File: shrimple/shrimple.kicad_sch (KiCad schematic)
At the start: 105 parts, among them U1 ProMicro

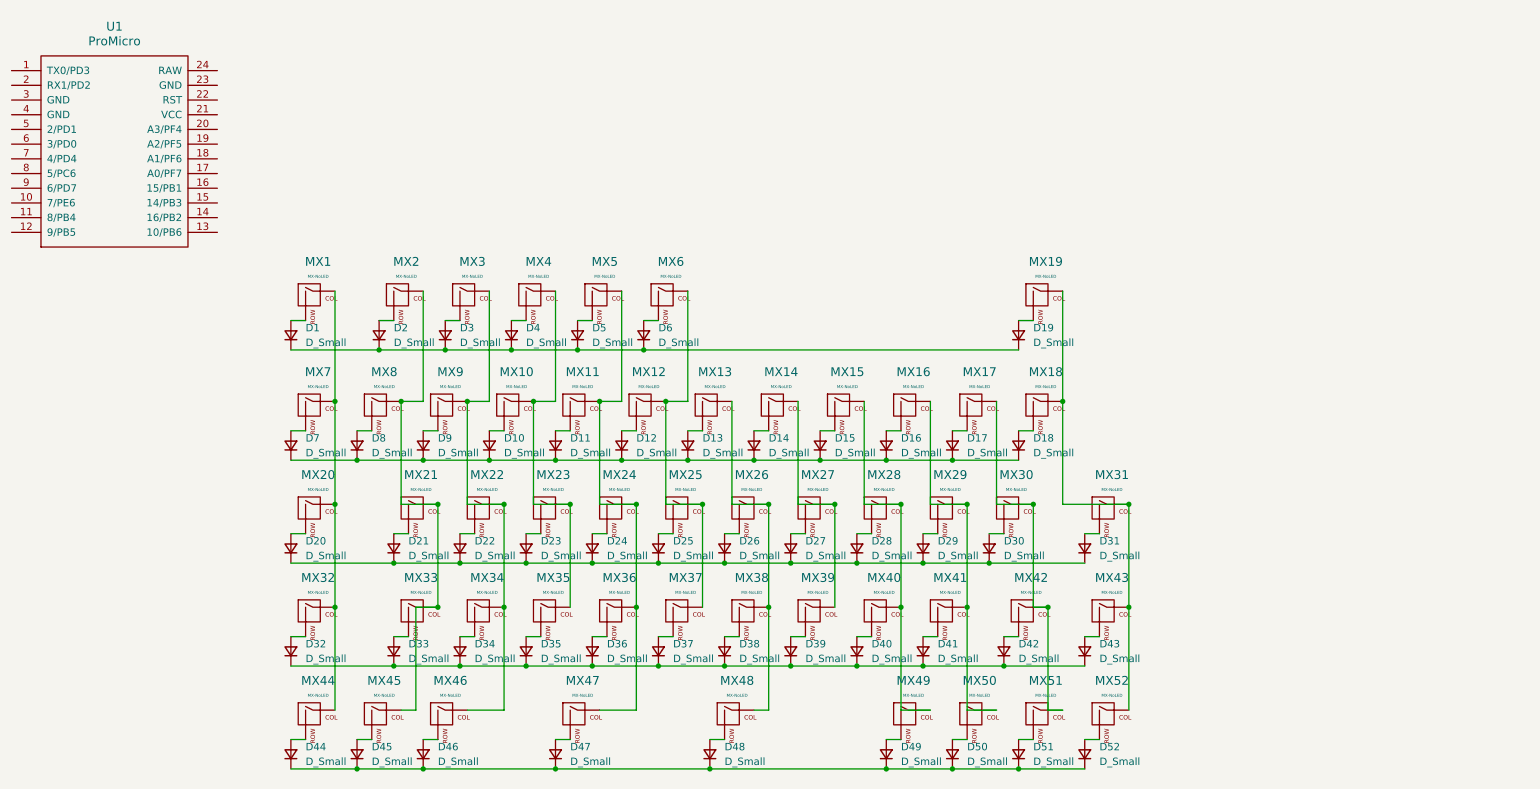
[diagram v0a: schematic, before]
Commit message: updated schematic and placed footprints
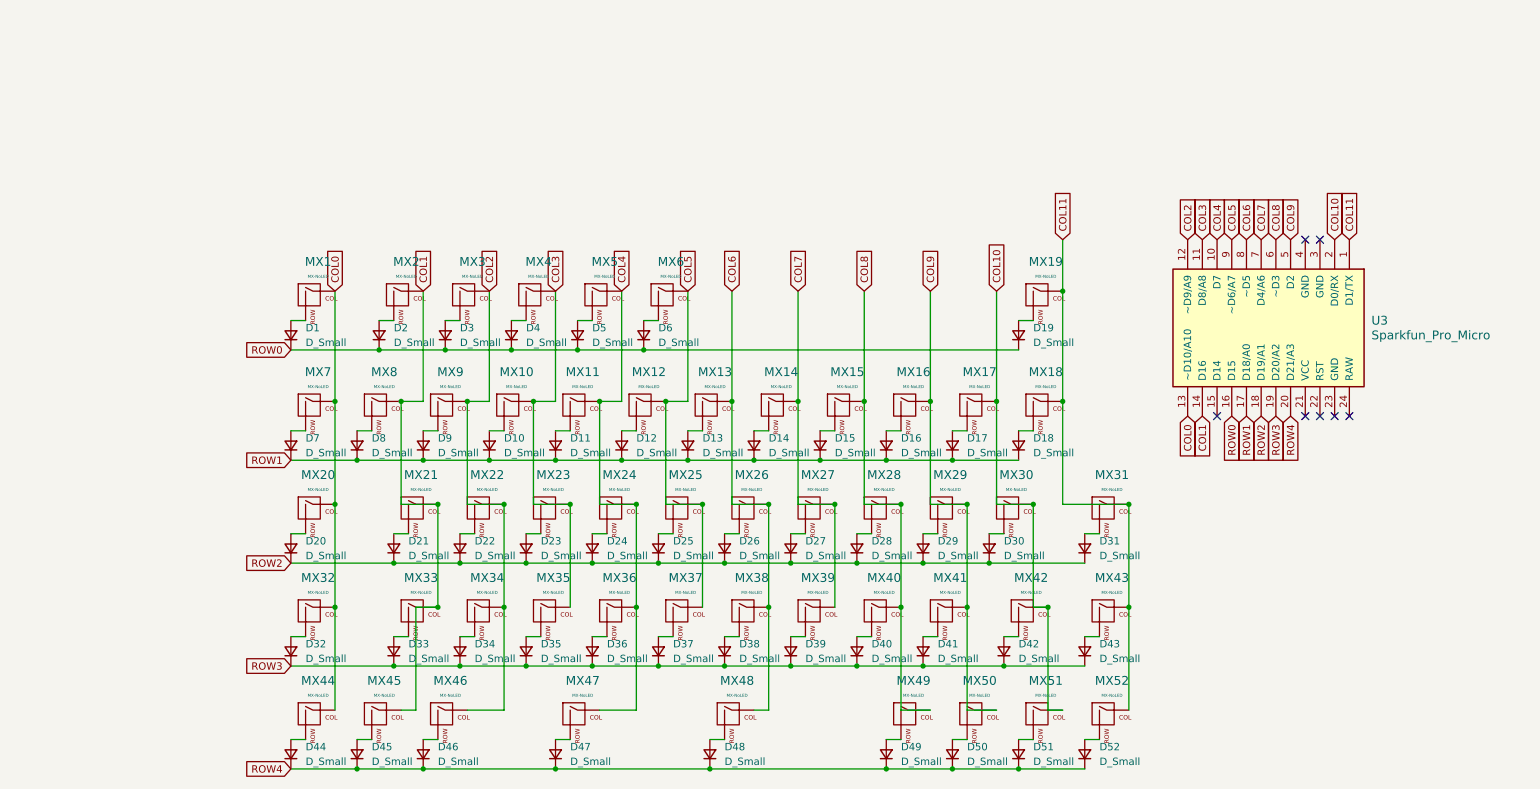
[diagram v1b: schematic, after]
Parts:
- removed U1: ProMicro, symbol keebio:ProMicro
- added U3: Sparkfun_Pro_Micro, arduino:Sparkfun_Pro_Micro, symbol arduino:Sparkfun_Pro_Micro
- D1, D10, D11, D12, D13, D14, D15, D16, D17, D18, D19, D2, D20, D21, D22, D23, D24, D25, D26, D27, D28, D29, D3, D30, D31, D32, D33, D34, D35, D36, D37, D38, D39, D4, D40, D41, D42, D43, D44, D45, D46, D47, D48, D49, D5, D50, D51, D52, D6, D7, D8, D9: footprint (none) -> Diode_SMD:D_SOD-123
- MX1, MX10, MX11, MX12, MX13, MX14, MX15, MX16, MX17, MX18, MX19, MX2, MX21, MX22, MX23, MX24, MX25, MX26, MX27, MX28, MX29, MX3, MX30, MX33, MX34, MX35, MX36, MX37, MX38, MX39, MX4, MX40, MX41, MX43, MX45, MX49, MX5, MX50, MX51, MX52, MX6, MX7, MX8, MX9: footprint (none) -> hybrids:MX-1U-NoLED
- MX20, MX31: footprint (none) -> hybrids:MX-1.5U-NoLED
- MX32: footprint (none) -> hybrids:MX-1.75U-NoLED
- MX42, MX44, MX46: footprint (none) -> hybrids:MX-1.25U-NoLED
- MX47: footprint (none) -> hybrids:MX-2.25U-ReversedStabilizers-NoLED
- MX48: footprint (none) -> hybrids:MX-2.75U-ReversedStabilizers-NoLED
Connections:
- net COL0: now reaches MX1.1 (COL), MX20.1 (COL), MX32.1 (COL), MX44.1 (COL), MX7.1 (COL)
- net COL0: now also U3.13 (~D10/A10)
- net COL3: now reaches MX10.1 (COL), MX23.1 (COL), MX35.1 (COL), MX4.1 (COL)
- net COL3: now also U3.11 (D8/A8)
- net ROW3: now reaches D32.1 (K), D33.1 (K), D34.1 (K), D35.1 (K), D36.1 (K), D37.1 (K), D38.1 (K), D39.1 (K), D40.1 (K), D41.1 (K), D42.1 (K), D43.1 (K)
- net ROW3: now also U3.19 (D20/A2)
- net ROW0: now reaches D1.1 (K), D19.1 (K), D2.1 (K), D3.1 (K), D4.1 (K), D5.1 (K), D6.1 (K)
- net ROW0: now also U3.16 (D15)
- net COL4: now reaches MX11.1 (COL), MX24.1 (COL), MX36.1 (COL), MX47.1 (COL), MX5.1 (COL)
- net COL4: now also U3.10 (D7)
- net COL7: now reaches MX14.1 (COL), MX27.1 (COL), MX39.1 (COL)
- net COL7: now also U3.7 (D4/A6)
- net ROW4: now reaches D44.1 (K), D45.1 (K), D46.1 (K), D47.1 (K), D48.1 (K), D49.1 (K), D50.1 (K), D51.1 (K), D52.1 (K)
- net ROW4: now also U3.20 (D21/A3)
- net COL9: now reaches MX16.1 (COL), MX29.1 (COL), MX41.1 (COL), MX50.1 (COL)
- net COL9: now also U3.5 (D2)
- net ROW1: now reaches D10.1 (K), D11.1 (K), D12.1 (K), D13.1 (K), D14.1 (K), D15.1 (K), D16.1 (K), D17.1 (K), D18.1 (K), D7.1 (K), D8.1 (K), D9.1 (K)
- net ROW1: now also U3.17 (D18/A0)
- net ROW2: now reaches D20.1 (K), D21.1 (K), D22.1 (K), D23.1 (K), D24.1 (K), D25.1 (K), D26.1 (K), D27.1 (K), D28.1 (K), D29.1 (K), D30.1 (K), D31.1 (K)
- net ROW2: now also U3.18 (D19/A1)
- net COL5: now reaches MX12.1 (COL), MX25.1 (COL), MX37.1 (COL), MX6.1 (COL)
- net COL5: now also U3.9 (~D6/A7)
- net COL2: now reaches MX22.1 (COL), MX3.1 (COL), MX34.1 (COL), MX46.1 (COL), MX9.1 (COL)
- net COL2: now also U3.12 (~D9/A9)
- net COL1: now reaches MX2.1 (COL), MX21.1 (COL), MX33.1 (COL), MX45.1 (COL), MX8.1 (COL)
- net COL1: now also U3.14 (D16)
- net COL11: now reaches MX18.1 (COL), MX19.1 (COL), MX31.1 (COL), MX43.1 (COL), MX52.1 (COL)
- net COL11: now also U3.1 (D1/TX)
- net COL6: now reaches MX13.1 (COL), MX26.1 (COL), MX38.1 (COL), MX48.1 (COL)
- net COL6: now also U3.8 (~D5)
- net COL10: now reaches MX17.1 (COL), MX30.1 (COL), MX42.1 (COL), MX51.1 (COL)
- net COL10: now also U3.2 (D0/RX)
- net COL8: now reaches MX15.1 (COL), MX28.1 (COL), MX40.1 (COL), MX49.1 (COL)
- net COL8: now also U3.6 (~D3)
- no-connect marks 0 -> 7

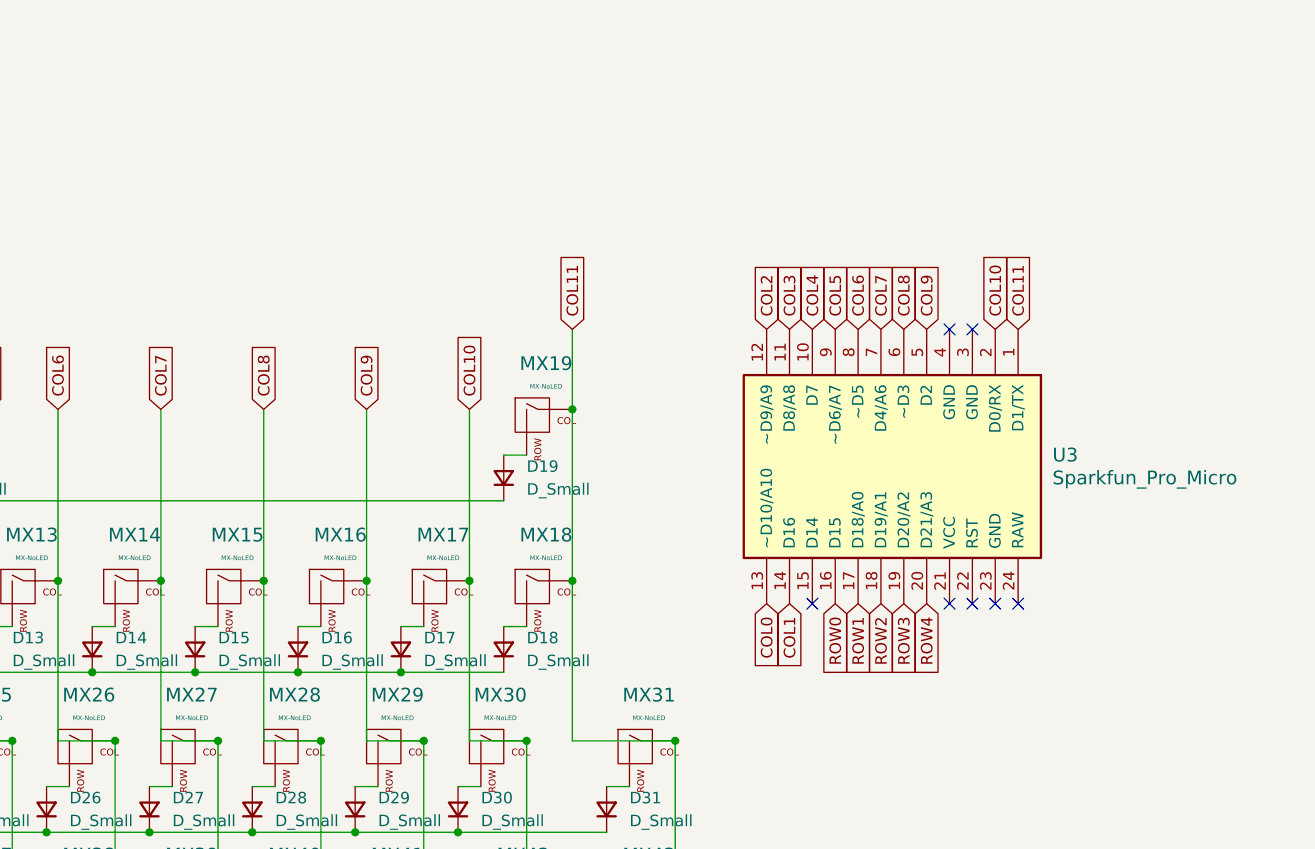
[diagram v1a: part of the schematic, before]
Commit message: added LED circuit
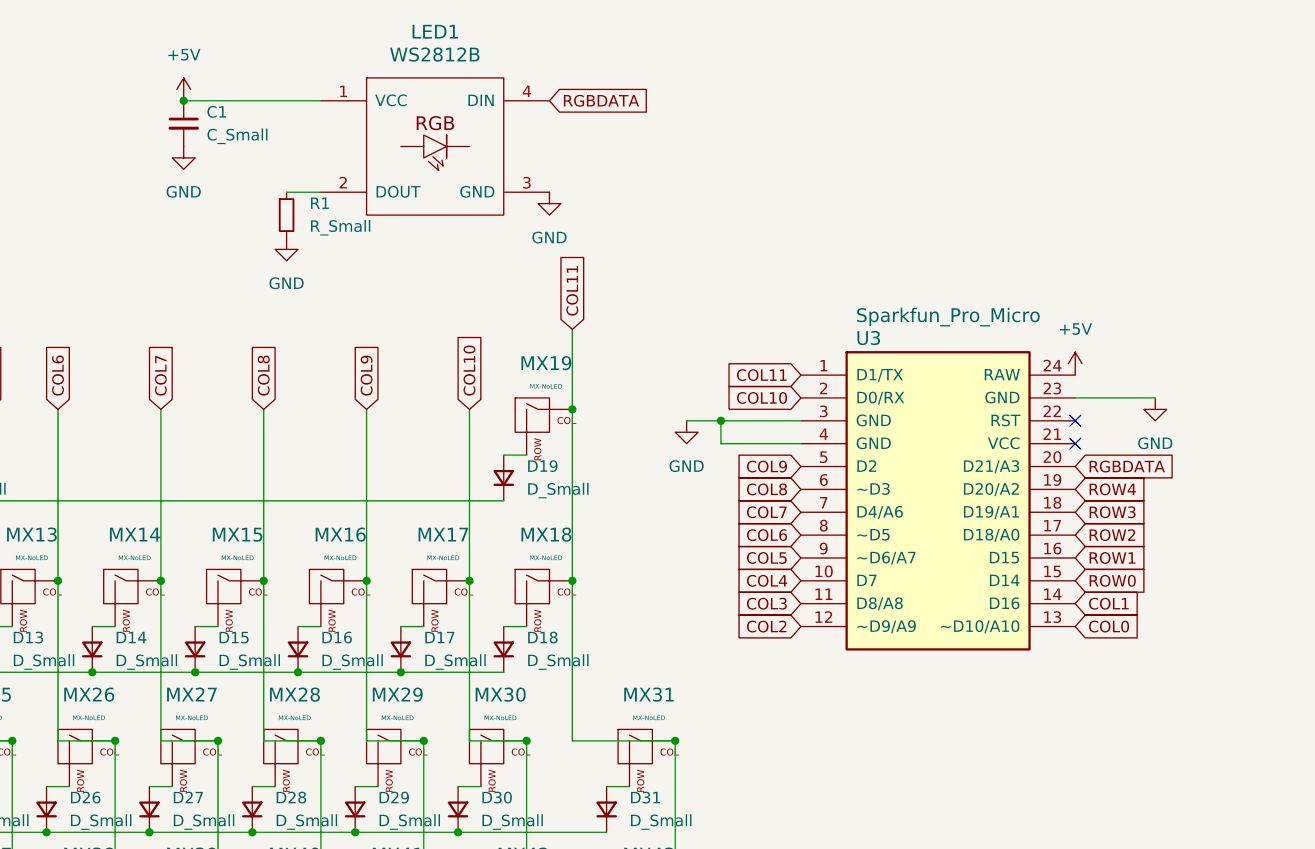
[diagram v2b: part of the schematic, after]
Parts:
- added C1: C_Small, Capacitor_SMD:C_0603_1608Metric_Pad1.08x0.95mm_HandSolder, symbol Device:C_Small
- added LED1: WS2812B, ws2812:WS2812B, symbol ws2182:WS2812B
- added R1: R_Small, Resistor_SMD:R_0805_2012Metric_Pad1.20x1.40mm_HandSolder, symbol Device:R_Small
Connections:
- net ROW0: now also U3.15 (D14); no longer U3.16 (D15)
- net ROW1: now also U3.16 (D15); no longer U3.17 (D18/A0)
- net ROW2: now also U3.17 (D18/A0); no longer U3.18 (D19/A1)
- net ROW3: now also U3.18 (D19/A1); no longer U3.19 (D20/A2)
- net ROW4: now also U3.19 (D20/A2); no longer U3.20 (D21/A3)
- net GND: now reaches U3.23 (GND)
- net GND: now also U3.3 (GND), U3.4 (GND), C1.2, LED1.3 (GND), R1.2
- net +5V: now reaches U3.24 (RAW)
- net +5V: now also C1.1, LED1.1 (VCC)
- new net: LED1.2 (DOUT), R1.1
- new net RGBDATA: LED1.4 (DIN), U3.20 (D21/A3)
- no-connect marks 7 -> 2
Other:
- moved on the sheet: U3

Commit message: added LED, routing attempt the first
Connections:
- net COL0: now also U3.7 (D4/A6); no longer U3.13 (~D10/A10)
- net COL1: now also U3.8 (~D5); no longer U3.14 (D16)
- net COL10: now also U3.13 (~D10/A10); no longer U3.2 (D0/RX)
- net COL2: now also U3.9 (~D6/A7); no longer U3.12 (~D9/A9)
- net COL3: now also U3.10 (D7); no longer U3.11 (D8/A8)
- net COL4: now also U3.11 (D8/A8); no longer U3.10 (D7)
- net COL5: now also U3.12 (~D9/A9); no longer U3.9 (~D6/A7)
- net COL6: now also U3.17 (D18/A0); no longer U3.8 (~D5)
- net COL7: now also U3.16 (D15); no longer U3.7 (D4/A6)
- net COL8: now also U3.15 (D14); no longer U3.6 (~D3)
- net COL9: now also U3.14 (D16); no longer U3.5 (D2)
- net ROW0: now also U3.6 (~D3); no longer U3.15 (D14)
- net ROW1: now also U3.18 (D19/A1); no longer U3.16 (D15)
- net ROW2: now also U3.19 (D20/A2); no longer U3.17 (D18/A0)
- net ROW3: now also U3.2 (D0/RX); no longer U3.18 (D19/A1)
- net ROW4: now also U3.5 (D2); no longer U3.19 (D20/A2)

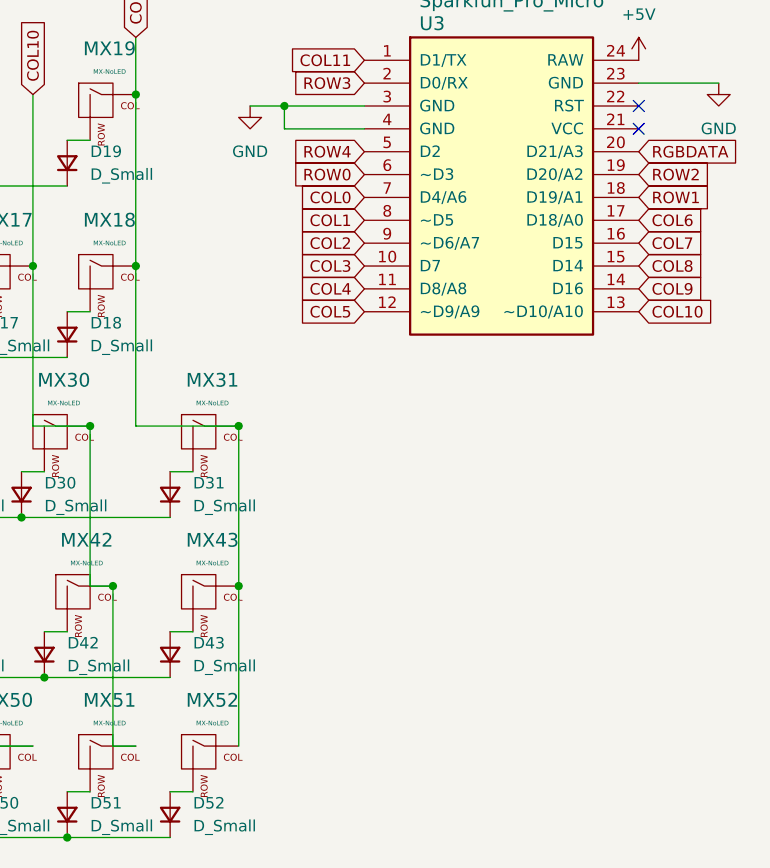
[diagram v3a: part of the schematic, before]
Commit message: fixed art and weird row trace
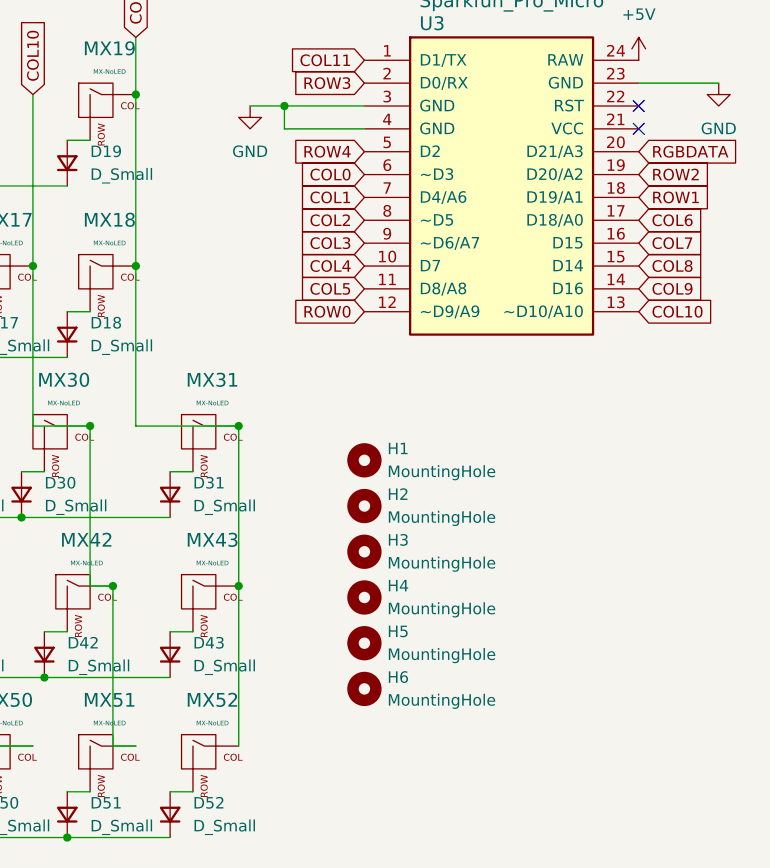
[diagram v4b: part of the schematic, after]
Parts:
- added H1, H2, H3, H4, H5, H6: MountingHole, MountingHole:MountingHole_2.2mm_M2_Pad_TopOnly, symbol Mechanical:MountingHole
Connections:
- net COL0: now also U3.6 (~D3); no longer U3.7 (D4/A6)
- net COL1: now also U3.7 (D4/A6); no longer U3.8 (~D5)
- net COL2: now also U3.8 (~D5); no longer U3.9 (~D6/A7)
- net COL3: now also U3.9 (~D6/A7); no longer U3.10 (D7)
- net COL4: now also U3.10 (D7); no longer U3.11 (D8/A8)
- net COL5: now also U3.11 (D8/A8); no longer U3.12 (~D9/A9)
- net ROW0: now also U3.12 (~D9/A9); no longer U3.6 (~D3)

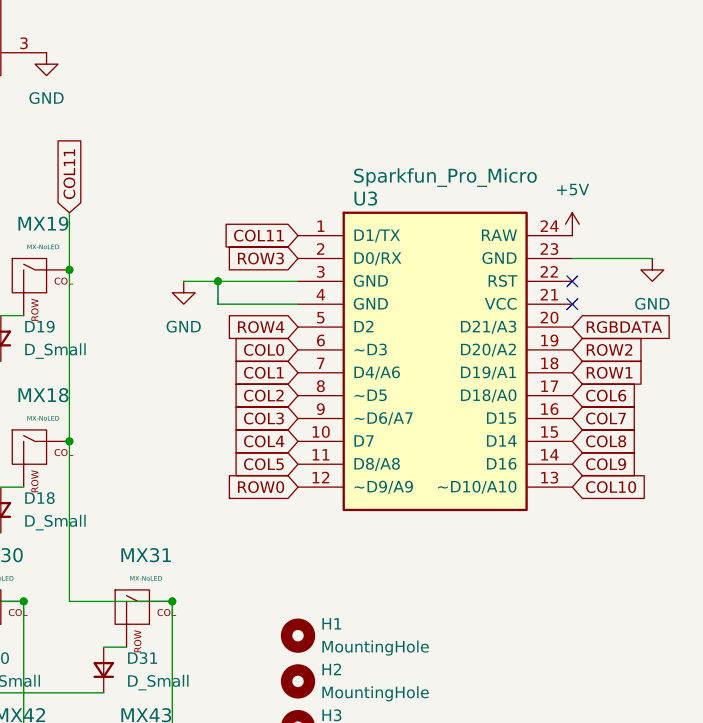
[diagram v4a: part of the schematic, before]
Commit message: changed mcu to aliexpress pro micro
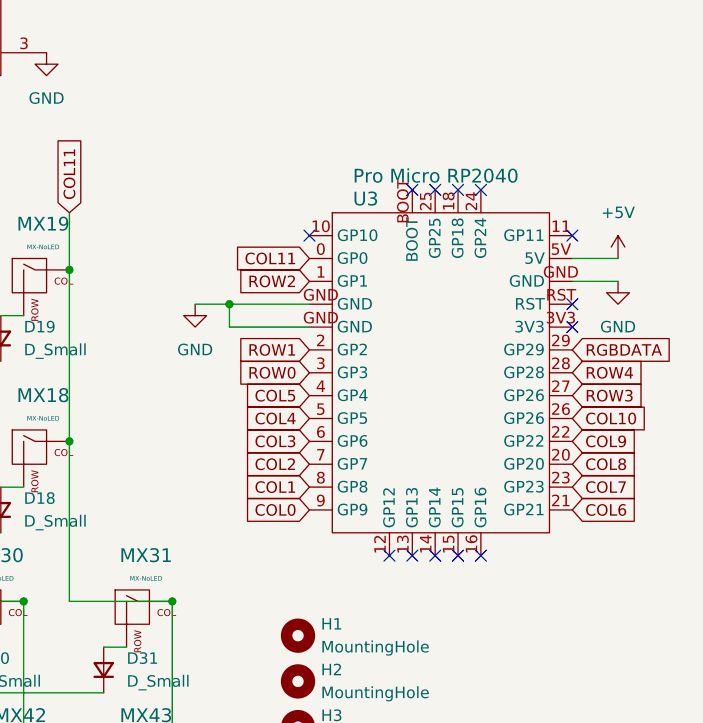
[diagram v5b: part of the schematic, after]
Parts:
- U3: value Sparkfun_Pro_Micro -> Pro Micro RP2040; footprint arduino:Sparkfun_Pro_Micro -> rp2040:pro_micro_rp2040; symbol arduino:Sparkfun_Pro_Micro -> promicro:pro_micro_rp2040
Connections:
- net +5V: now also U3.5V; no longer U3.24 (RAW)
- net COL0: now also U3.9 (GP9); no longer U3.6 (~D3)
- net COL1: now also U3.8 (GP8); no longer U3.7 (D4/A6)
- net COL10: now also U3.26 (GP26); no longer U3.13 (~D10/A10)
- net COL11: now also U3.0 (GP0); no longer U3.1 (D1/TX)
- net COL2: now also U3.7 (GP7); no longer U3.8 (~D5)
- net COL3: now also U3.6 (GP6); no longer U3.9 (~D6/A7)
- net COL4: now also U3.5 (GP5); no longer U3.10 (D7)
- net COL5: now also U3.4 (GP4); no longer U3.11 (D8/A8)
- net COL6: now also U3.21 (GP21); no longer U3.17 (D18/A0)
- net COL7: now also U3.23 (GP23); no longer U3.16 (D15)
- net COL8: now also U3.20 (GP20); no longer U3.15 (D14)
- net COL9: now also U3.22 (GP22); no longer U3.14 (D16)
- net GND: now also U3.GND; no longer U3.23 (GND), U3.3 (GND), U3.4 (GND)
- net RGBDATA: now also U3.29 (GP29); no longer U3.20 (D21/A3)
- net ROW0: now also U3.3 (GP3); no longer U3.12 (~D9/A9)
- net ROW1: now also U3.2 (GP2); no longer U3.18 (D19/A1)
- net ROW2: now also U3.1 (GP1); no longer U3.19 (D20/A2)
- net ROW3: now also U3.27 (GP26); no longer U3.2 (D0/RX)
- net ROW4: now also U3.28 (GP28); no longer U3.5 (D2)
- no-connect marks 2 -> 13
